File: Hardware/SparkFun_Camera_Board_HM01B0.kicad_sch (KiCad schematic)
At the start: 43 parts, among them J1 Conn_01x09, J2 Conn_01x09, J3 Conn_01x09, J4 HM01B0, Q1 RE1C002UNTCL, Q2 RE1C002UNTCL, U1 HM0360, U2 RT9080-1.2V, U3 RT9080-2.8V, Y1 24MHz

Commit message: Actually save the schematic...
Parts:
- added Q3, Q4: RE1C002UNTCL, SparkFun-Semiconductor-Standard:SC-89 SOT-490, symbol SparkFun-DiscreteSemi:Q_NMOS_0.2A_20V
- added R9: 100k, SparkFun-Resistor:R_0603_1608Metric, symbol SparkFun-Resistor:100k_0603
- U1: value HM0360 -> HM01B0; footprint lcd-tft:HM0360 -> lcd-tft:HM01B0-ANA-00FT870; symbol HM0360:HM0360 -> HM0360:HM01B0-ANA-00FT870
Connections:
- net 2.8V: now also JP7.2 (B); no longer R5.2, R6.2, R7.2
- net 3.3V: now also R9.1; no longer U2.3 (EN), U3.3 (EN)
- net GND: now also D1.1 (K), R5.1, R6.1, Q3.2 (S), Q4.2 (S); no longer JP7.1 (A)
- net CAM_~{PWDN} renamed CAM_PWDN
- net CAM_PWDN: now also R5.2, Q3.1 (G); no longer R6.1
- net CAM_~{RST} renamed CAM_RST
- net CAM_RST: now also R6.2, Q4.1 (G); no longer R5.1
- new net: JP7.1 (A), R7.2
- new net EN: Q3.3 (D), Q4.3 (D), R9.2, U2.3 (EN), U3.3 (EN)
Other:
- note added: "Power Control"
- moved on the sheet: C6, C7, C8, D1, J4, R5, R6, R7, TP1, TP2, U1

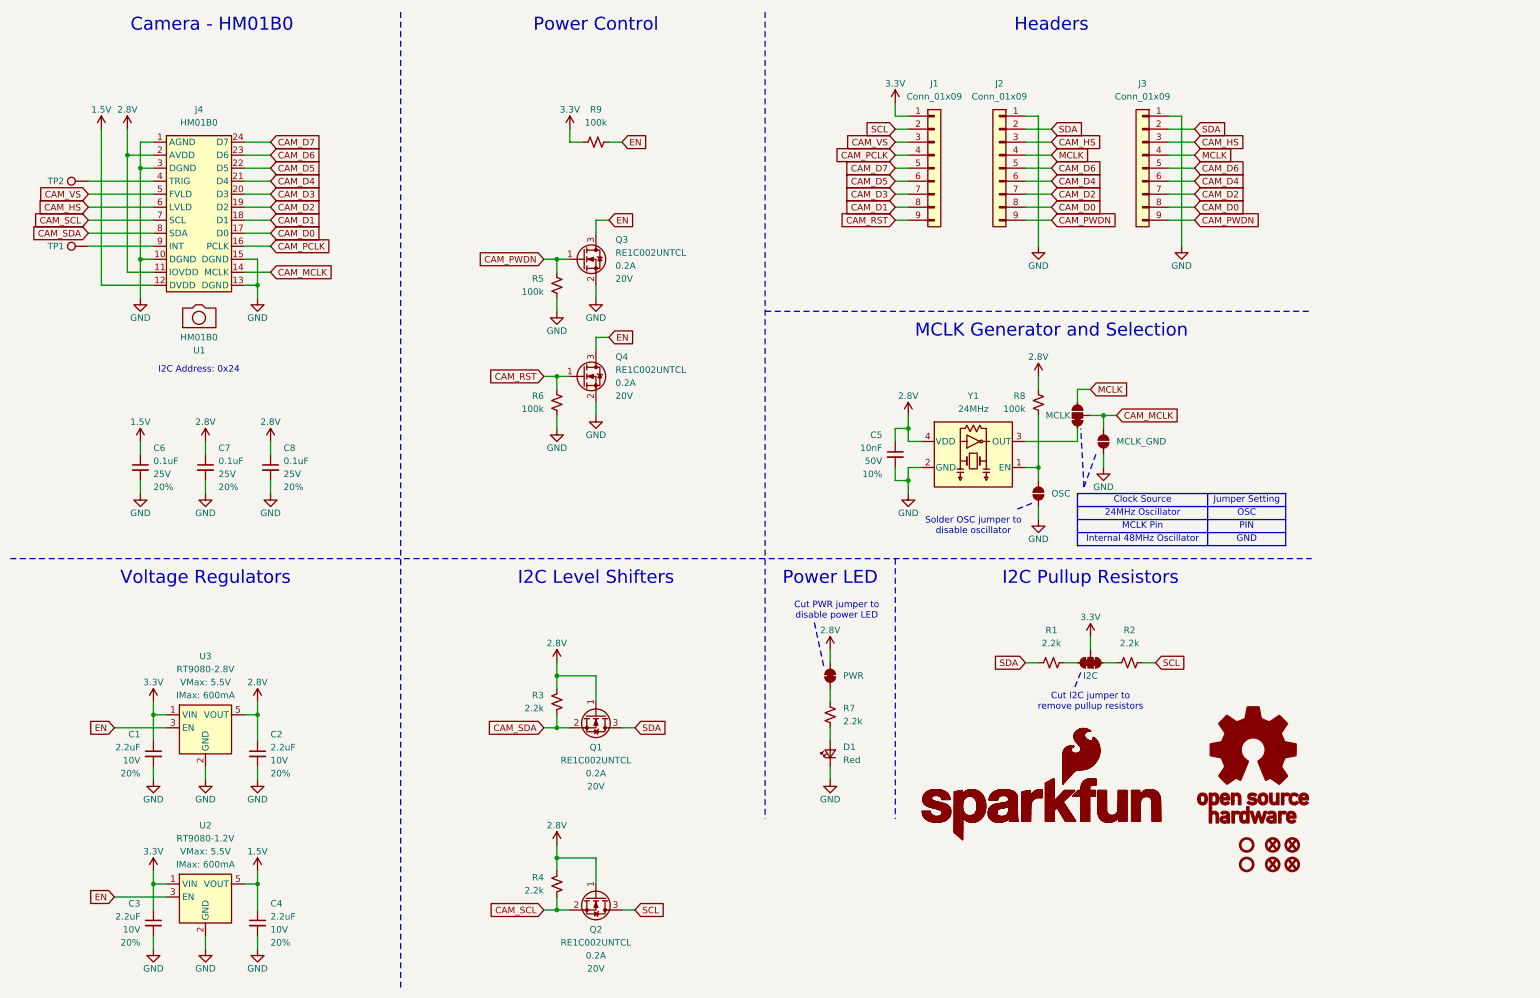
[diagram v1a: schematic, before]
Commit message: Design review updates
Rearrange power control circuitry in schematic
Add note to MCLK jumper in schematic
Change camera connector silk pin labels
Improve GND continuity
Increase thermal spoke width
Change In2.Cu to 2.8V instead of GND
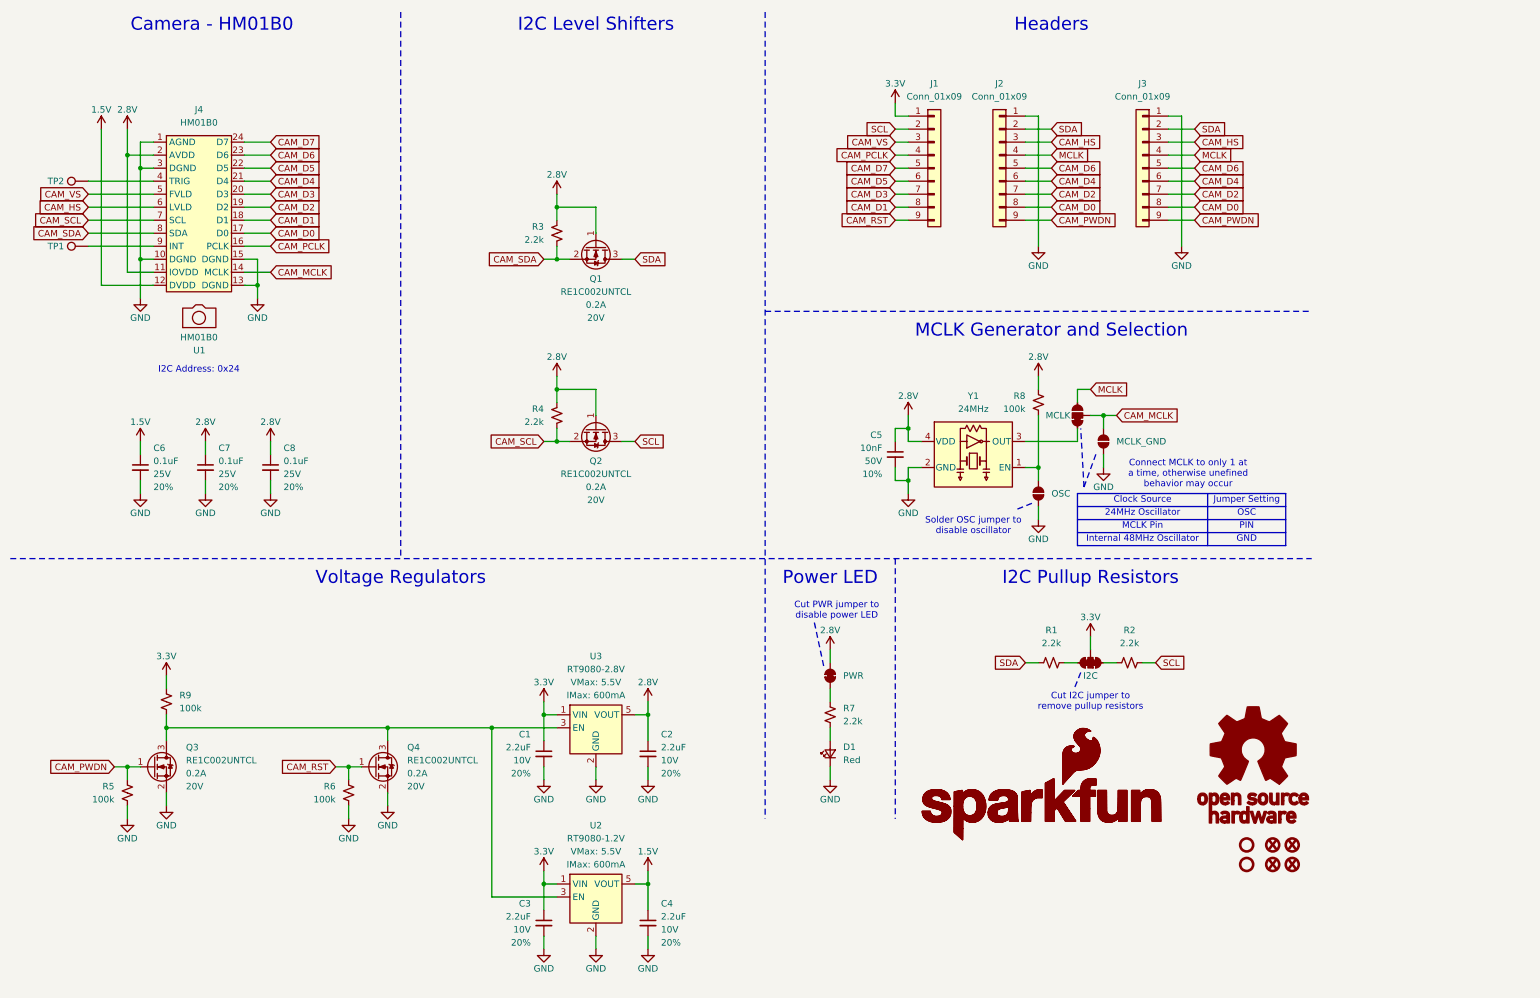
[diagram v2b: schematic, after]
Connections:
- net EN: no longer names the net of Q3.3 (D), Q4.3 (D), R9.2, U2.3 (EN), U3.3 (EN)
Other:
- note added: "Connect MCLK to only 1 at a time, otherwise unefined behavior may occur"
- note removed: "Power Control"
- moved on the sheet: C1, C2, C3, C4, Q1, Q2, Q3, Q4, R3, R4, R5, R6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

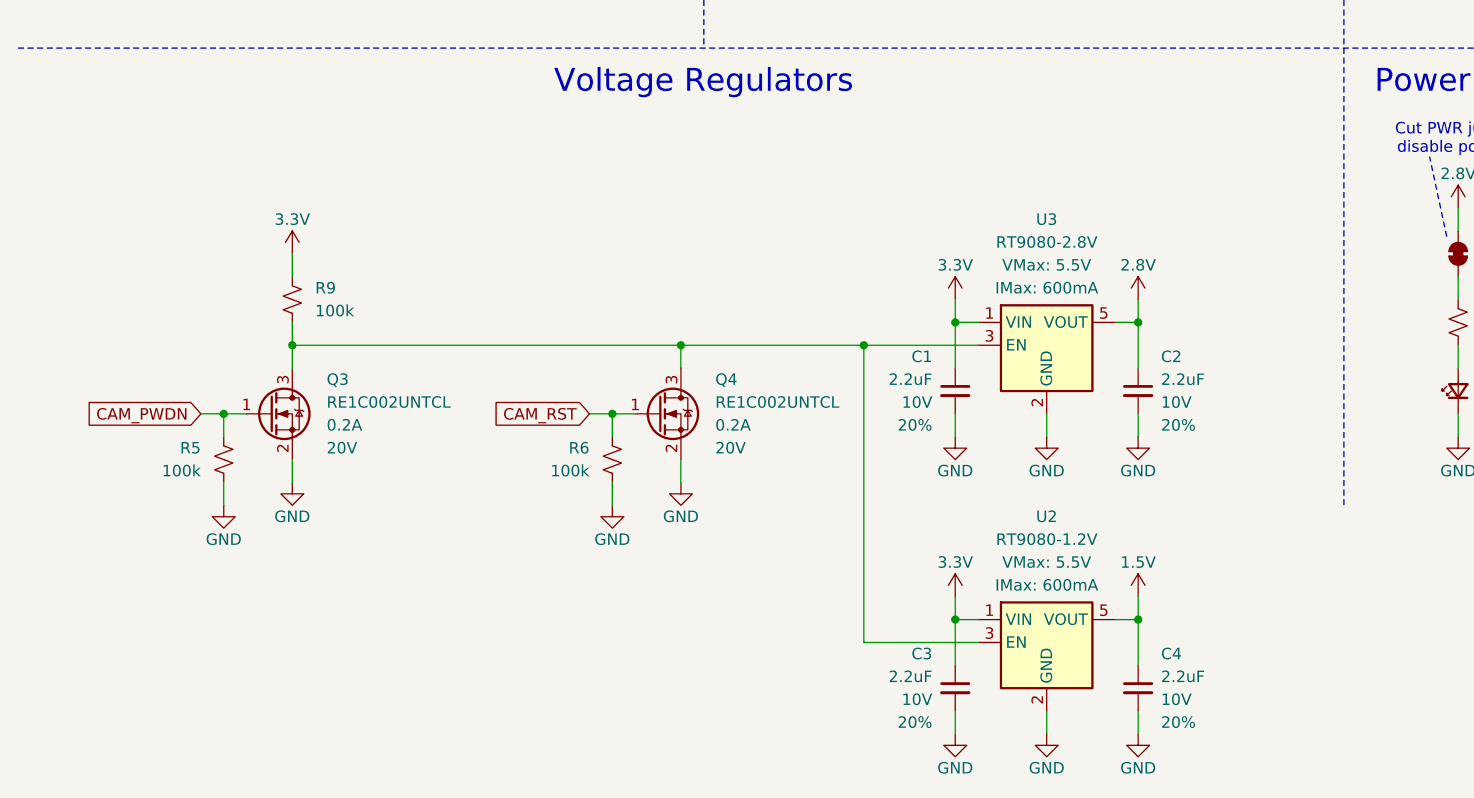
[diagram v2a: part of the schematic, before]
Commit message: Change regulators to adjustable type
Using adjustable regulators at least for prototypes. May change back to fixed regulators depending on testing
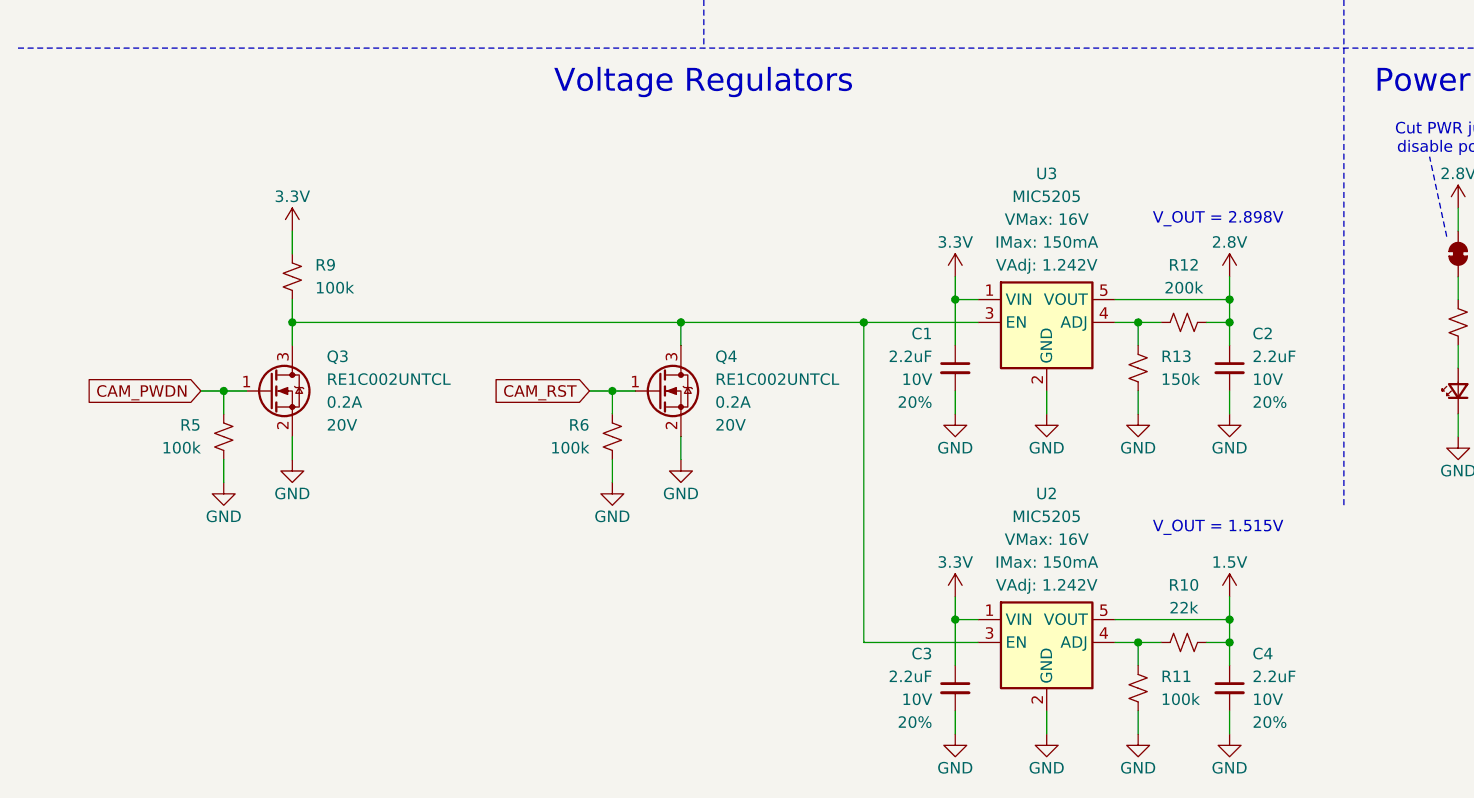
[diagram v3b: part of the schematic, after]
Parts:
- removed U2: RT9080-1.2V, SparkFun-Semiconductor-Standard:SOT23-5, symbol SparkFun-Regulator:RT9080-1.2
- removed U3: RT9080-2.8V, SparkFun-Semiconductor-Standard:SOT23-5, symbol SparkFun-Regulator:RT9080-2.8
- added R10: 22k, SparkFun-Resistor:R_0603_1608Metric, symbol SparkFun-Resistor:22k_0603
- added R11: 100k, SparkFun-Resistor:R_0603_1608Metric, symbol SparkFun-Resistor:100k_0603
- added R12: 200k, SparkFun-Resistor:R_0603_1608Metric, symbol SparkFun-Resistor:200k_0603
- added R13: 150k, SparkFun-Resistor:R_0603_1608Metric, symbol SparkFun-Resistor:150k_0603
- added U2, U3: MIC5205, SparkFun-Semiconductor-Standard:SOT23-5, symbol SparkFun-Regulator:MIC5205
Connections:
- net 1.5V: now also R10.2, U2.5 (VOUT)
- net 2.8V: now also R12.2, U3.5 (VOUT)
- net 3.3V: now also U2.1 (VIN), U3.1 (VIN)
- net GND: now also R11.1, R13.1, U2.2 (GND), U3.2 (GND)
- net at Q3.3 (D), Q4.3 (D), R9.2: now also U2.3 (EN), U3.3 (EN)
- new net: R12.1, R13.2, U3.4 (ADJ)
- new net: R10.1, R11.2, U2.4 (ADJ)
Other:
- note added: "V_OUT = 1.515V"
- note added: "V_OUT = 2.898V"
- moved on the sheet: C1, C2, C4, Q3, Q4, R5, R6, R9

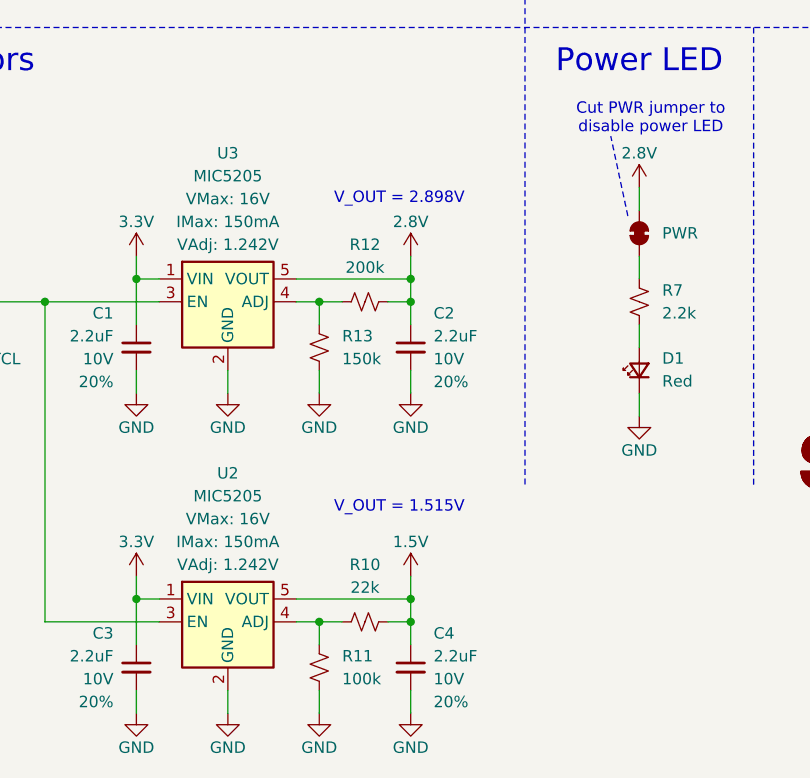
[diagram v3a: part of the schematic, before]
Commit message: Fix voltage regulator resistor orders
Reference voltage is relative to VOUT instead  of GND. Why???
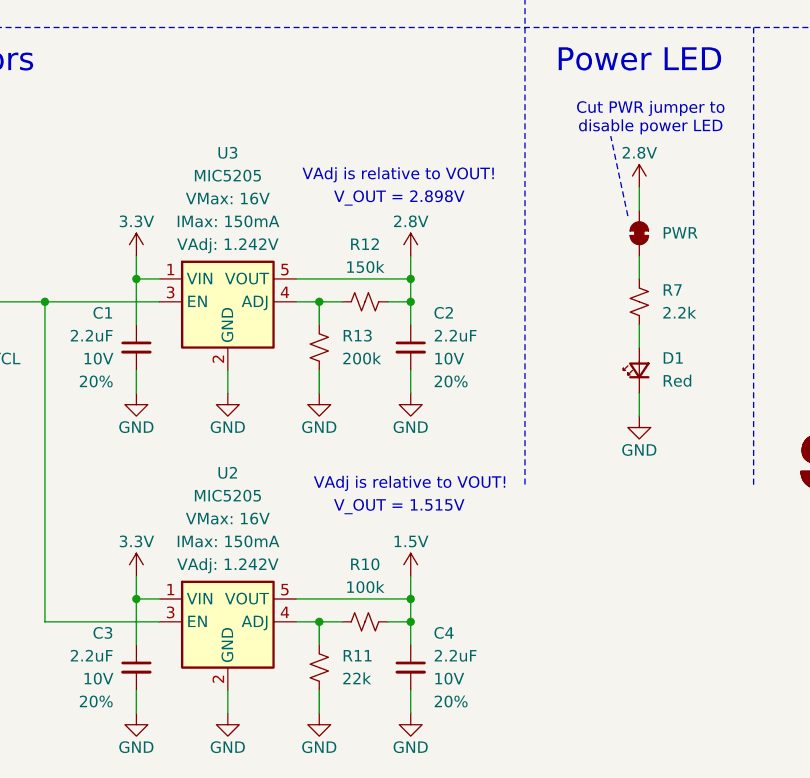
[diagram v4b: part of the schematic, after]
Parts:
- R10: value 22k -> 100k; symbol SparkFun-Resistor:22k_0603 -> SparkFun-Resistor:100k_0603; PROD_ID RES-07853 -> RES-07828
- R11: value 100k -> 22k; symbol SparkFun-Resistor:100k_0603 -> SparkFun-Resistor:22k_0603; PROD_ID RES-07828 -> RES-07853
- R12: value 200k -> 150k; symbol SparkFun-Resistor:200k_0603 -> SparkFun-Resistor:150k_0603; PROD_ID RES-09385 -> RES-09117
- R13: value 150k -> 200k; symbol SparkFun-Resistor:150k_0603 -> SparkFun-Resistor:200k_0603; PROD_ID RES-09117 -> RES-09385
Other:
- note added: "VAdj is relative to VOUT!"
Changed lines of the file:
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@@
 		)
 	)
+	(text "VAdj is relative to VOUT!"
+		(exclude_from_sim no)
+		(at 146.05 135.89 0)
+		(effects
+			(font
+				(size 1.27 1.27)
+			)
+		)
+	)
 	(text "Camera - HM01B0"
 		(exclude_from_sim no)
@@
 		)
 	)
+	(text "VAdj is relative to VOUT!"
+		(exclude_from_sim no)
+		(at 147.32 170.18 0)
+		(effects
+			(font
+				(size 1.27 1.27)
+			)
+		)
+	)
 	(text "Power LED"
 		(exclude_from_sim no)
@@
 	)
 	(symbol
-		(lib_id "SparkFun-Resistor:200k_0603")
+		(lib_id "SparkFun-Resistor:150k_0603")
 		(at 142.24 149.86 0)
 		(unit 1)
@@
 			)
 		)
-		(property "Value" "200k"
+		(property "Value" "150k"
 			(at 142.24 146.05 0)
 			(effects
@@
 			)
 		)
-		(property "PROD_ID" "RES-09385"
+		(property "PROD_ID" "RES-09117"
 			(at 142.24 156.718 0)
 			(effects
@@
 	)
 	(symbol
-		(lib_id "SparkFun-Resistor:100k_0603")
+		(lib_id "SparkFun-Resistor:22k_0603")
 		(at 137.16 190.5 90)
 		(unit 1)
@@
 			)
 		)
-		(property "Value" "100k"
+		(property "Value" "22k"
 			(at 139.7 191.7699 90)
 			(effects
@@
 		)
 		(property "Footprint" "SparkFun-Resistor:R_0603_1608Metric"
-			(at 141.478 190.5 0)
+			(at 141.732 190.5 0)
 			(effects
 				(font
@@
 			)
 		)
-		(property "PROD_ID" "RES-07828"
-			(at 143.51 190.5 0)
+		(property "PROD_ID" "RES-07853"
+			(at 144.018 190.5 0)
 			(effects
 				(font
@@
 	)
 	(symbol
-		(lib_id "SparkFun-Resistor:22k_0603")
+		(lib_id "SparkFun-Resistor:100k_0603")
 		(at 142.24 185.42 0)
 		(unit 1)
@@
 			)
 		)
-		(property "Value" "22k"
+		(property "Value" "100k"
 			(at 142.24 181.61 0)
 			(effects
@@
 		)
 		(property "Footprint" "SparkFun-Resistor:R_0603_1608Metric"
-			(at 142.24 189.992 0)
+			(at 142.24 189.738 0)
 			(effects
 				(font
@@
 			)
 		)
-		(property "PROD_ID" "RES-07853"
-			(at 142.24 192.278 0)
+		(property "PROD_ID" "RES-07828"
+			(at 142.24 191.77 0)
 			(effects
 				(font
@@
 	)
 	(symbol
-		(lib_id "SparkFun-Resistor:150k_0603")
+		(lib_id "SparkFun-Resistor:200k_0603")
 		(at 137.16 154.94 90)
 		(unit 1)
@@
 			)
 		)
-		(property "Value" "150k"
+		(property "Value" "200k"
 			(at 139.7 156.2099 90)
 			(effects
@@
 			)
 		)
-		(property "PROD_ID" "RES-09117"
+		(property "PROD_ID" "RES-09385"
 			(at 144.018 154.94 0)
 			(effects

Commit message: Fix HM01B0 PROD_ID
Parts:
- U1: PROD_ID SEN-25501 -> SEN-25897
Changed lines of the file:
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@@
 			)
 		)
-		(property "PROD_ID" "SEN-25501"
+		(property "PROD_ID" "SEN-25897"
 			(at 49.53 78.74 0)
 			(effects
